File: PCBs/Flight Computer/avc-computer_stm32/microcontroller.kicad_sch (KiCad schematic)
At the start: 12 parts, among them J1 Conn_ARM_JTAG_SWD_10, U3 STM32F103C8Tx

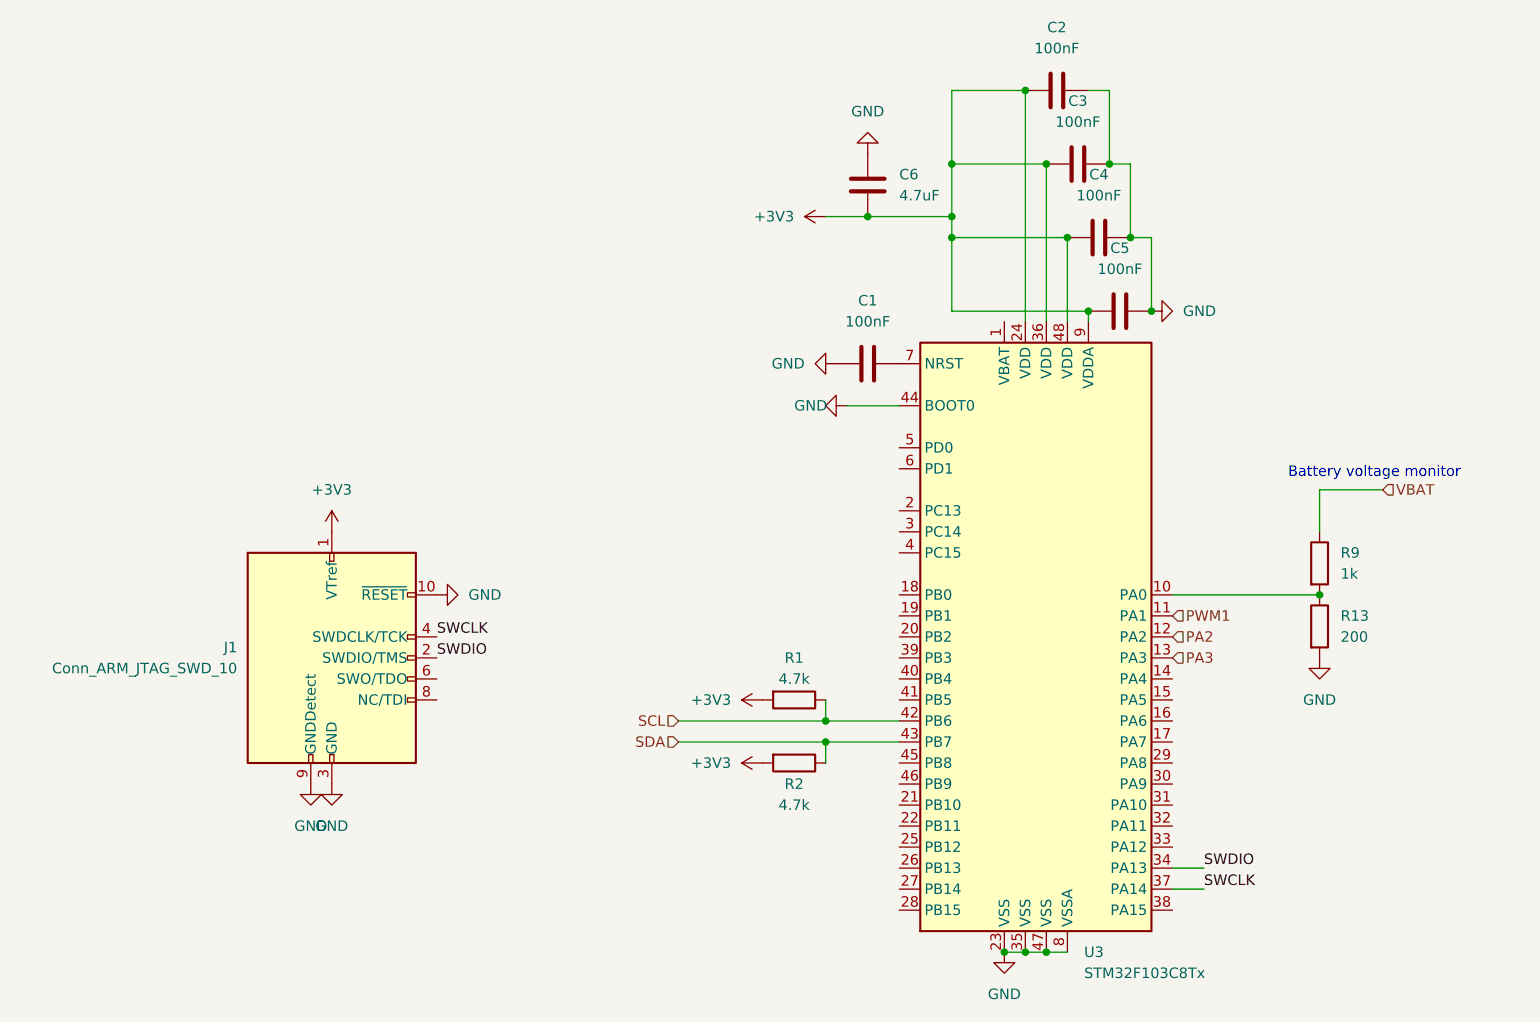
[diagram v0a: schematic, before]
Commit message: Began fixing reference designators
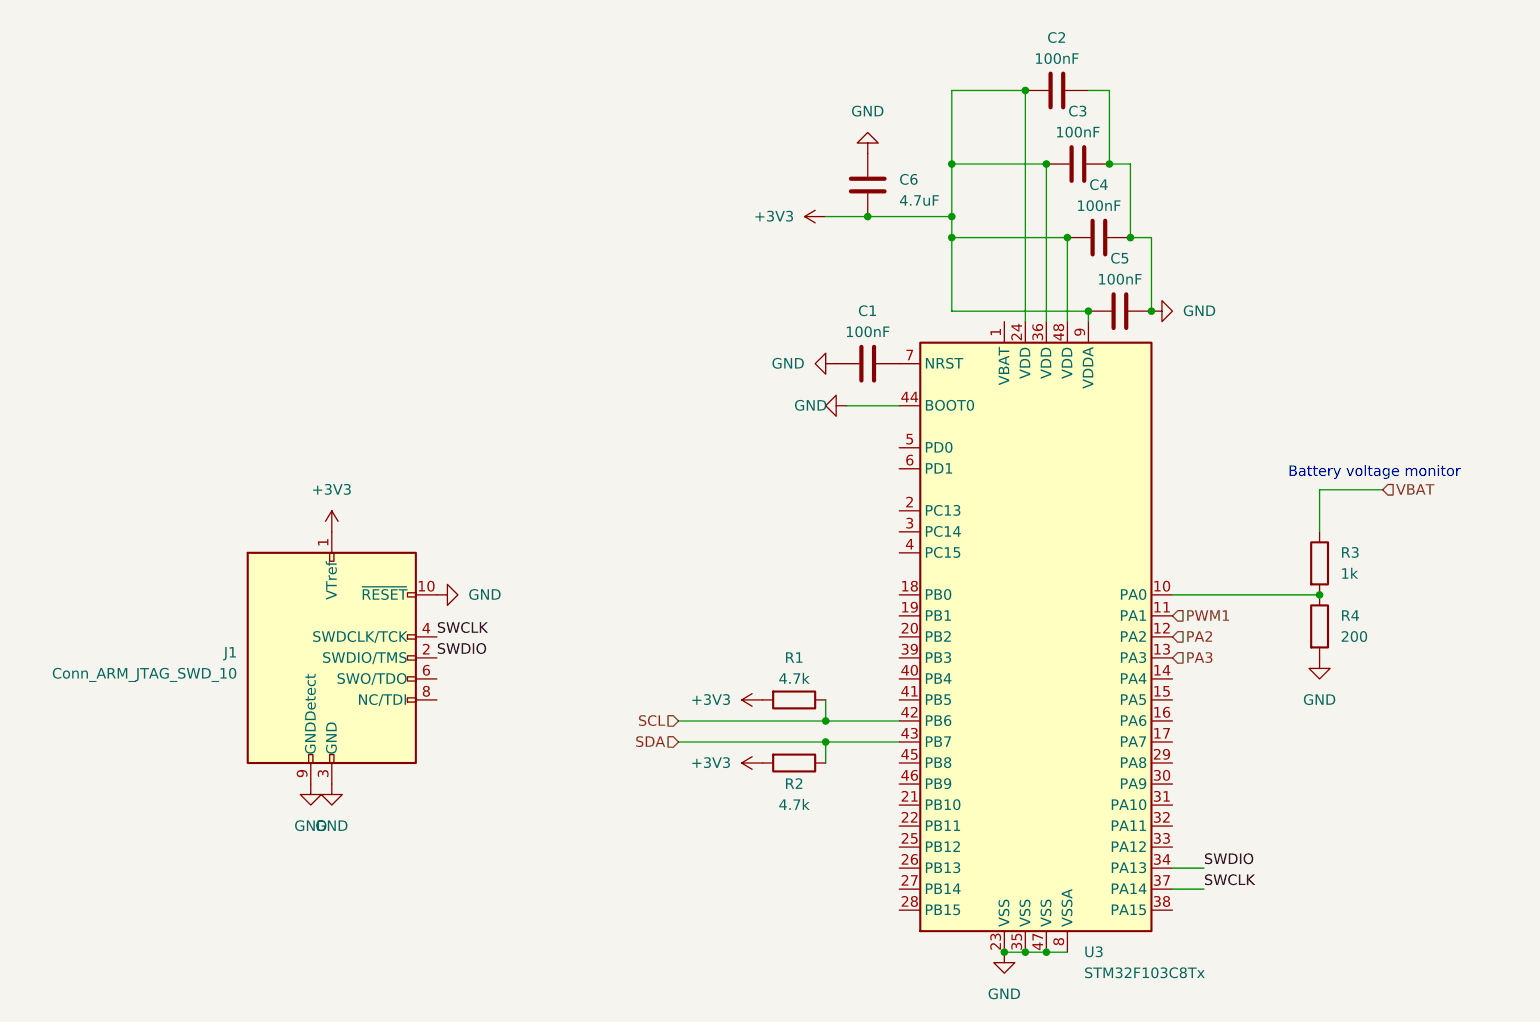
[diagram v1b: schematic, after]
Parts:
- renumbered R9 to R3, R13 to R4

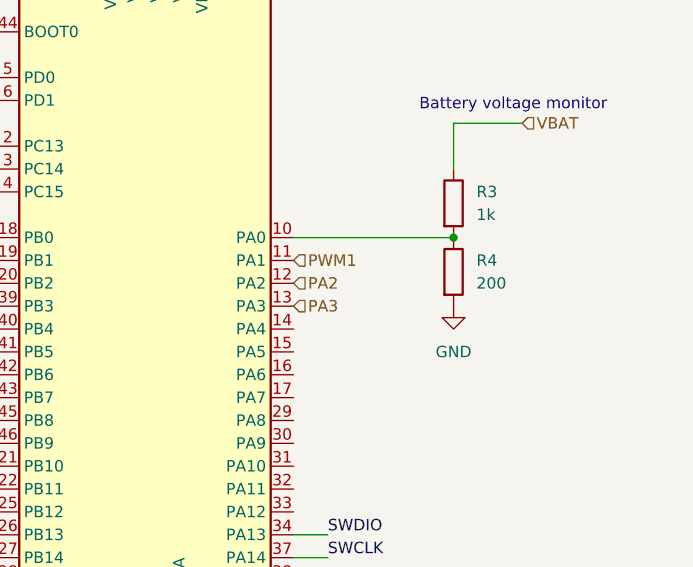
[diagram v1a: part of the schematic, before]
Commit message: Relpaced swithcing regulator with linear regulator. Removed unneccesary components. Replaced barometric pressure sensor with better one. Added connectors for brake servo & hall effect sensor
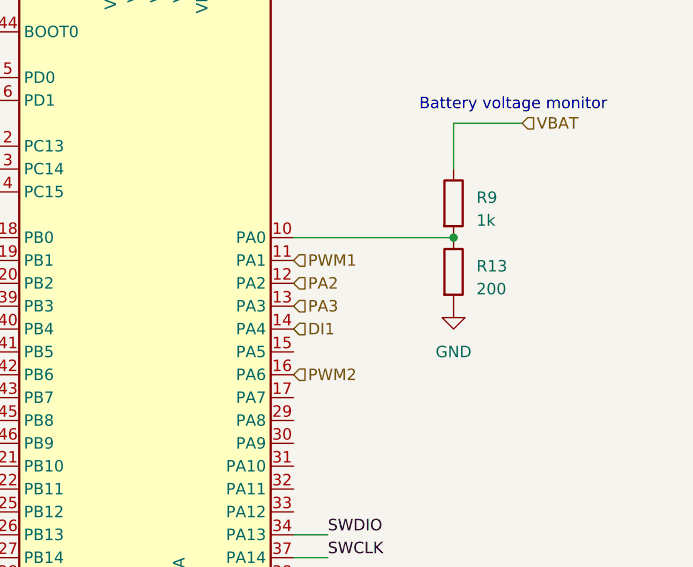
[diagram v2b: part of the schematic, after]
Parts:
- renumbered R4 to R13, R3 to R9
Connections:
- net DI1: now reaches U3.14 (PA4)
- net PWM2: now reaches U3.16 (PA6)
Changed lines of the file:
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@@
     (effects (font (size 1.27 1.27)) (justify right))
+  )
+  (hierarchical_label "PWM2" (shape input) (at 167.64 97.79 0) (fields_autoplaced)
+    (effects (font (size 1.27 1.27)) (justify left))
+  )
+  (hierarchical_label "DI1" (shape input) (at 167.64 92.71 0) (fields_autoplaced)
+    (effects (font (size 1.27 1.27)) (justify left))
   )
   (hierarchical_label "SDA" (shape input) (at 107.95 100.33 180) (fields_autoplaced)
@@
   (symbol (lib_id "Device:R") (at 185.42 86.36 0) (unit 1)
     (in_bom yes) (on_board yes) (dnp no) (fields_autoplaced)
-    (property "Reference" "R4" (at 187.96 85.0899 0)
-      (effects (font (size 1.27 1.27)) (justify left))
-    )
-    (property "Value" "200" (at 187.96 87.6299 0)
+    (property "Reference" "R13" (at 187.96 85.725 0)
+      (effects (font (size 1.27 1.27)) (justify left))
+    )
+    (property "Value" "200" (at 187.96 88.265 0)
       (effects (font (size 1.27 1.27)) (justify left))
     )
@@
       (project "avc-computer"
         (path "/e63e39d7-6ac0-4ffd-8aa3-1841a4541b55/1cc7165a-e701-4677-b265-806db2aaedf3"
-          (reference "R4") (unit 1)
+          (reference "R13") (unit 1)
         )
       )
@@
   (symbol (lib_id "Device:R") (at 185.42 78.74 0) (unit 1)
     (in_bom yes) (on_board yes) (dnp no) (fields_autoplaced)
-    (property "Reference" "R3" (at 187.96 77.4699 0)
-      (effects (font (size 1.27 1.27)) (justify left))
-    )
-    (property "Value" "1k" (at 187.96 80.0099 0)
+    (property "Reference" "R9" (at 187.96 78.105 0)
+      (effects (font (size 1.27 1.27)) (justify left))
+    )
+    (property "Value" "1k" (at 187.96 80.645 0)
       (effects (font (size 1.27 1.27)) (justify left))
     )
@@
       (project "avc-computer"
         (path "/e63e39d7-6ac0-4ffd-8aa3-1841a4541b55/1cc7165a-e701-4677-b265-806db2aaedf3"
-          (reference "R3") (unit 1)
-        )
-      )
+          (reference "R9") (unit 1)
+        )
+      )
